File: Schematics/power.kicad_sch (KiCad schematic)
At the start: 12 parts, among them Q6 Q_PMOS_GSD, U3 PowerIn, U4 LDL1117-3.3

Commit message: updated to KiCad 10.0, updated .gitignore
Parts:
- C19: LCSC C2932476 -> C15850
- R30: LCSC C2933415 -> C17713
- U3: now left out of the parts list
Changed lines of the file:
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@@
 		(unit 1)
 		(exclude_from_sim no)
-		(in_bom yes)
+		(in_bom no)
 		(on_board yes)
 		(dnp no)
@@
 			)
 		)
-		(property "LCSC" "C2933415"
+		(property "LCSC" "C17713"
 			(at 99.06 86.36 0)
 			(effects
@@
 			)
 		)
-		(property "LCSC" "C2932476"
+		(property "LCSC" "C15850"
 			(at 210.82 105.41 0)
 			(effects

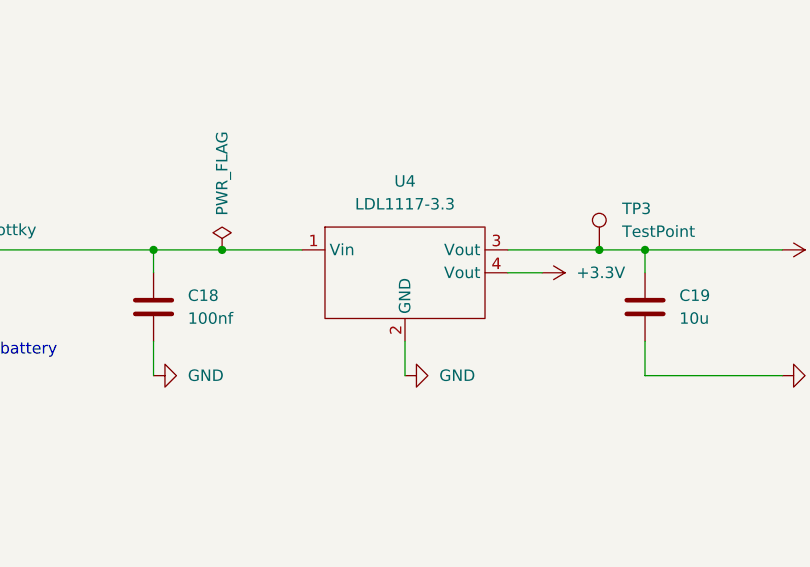
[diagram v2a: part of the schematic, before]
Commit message: Fixing ldo pinout, updated lora drivers need to still write final function such as lora sleep ect
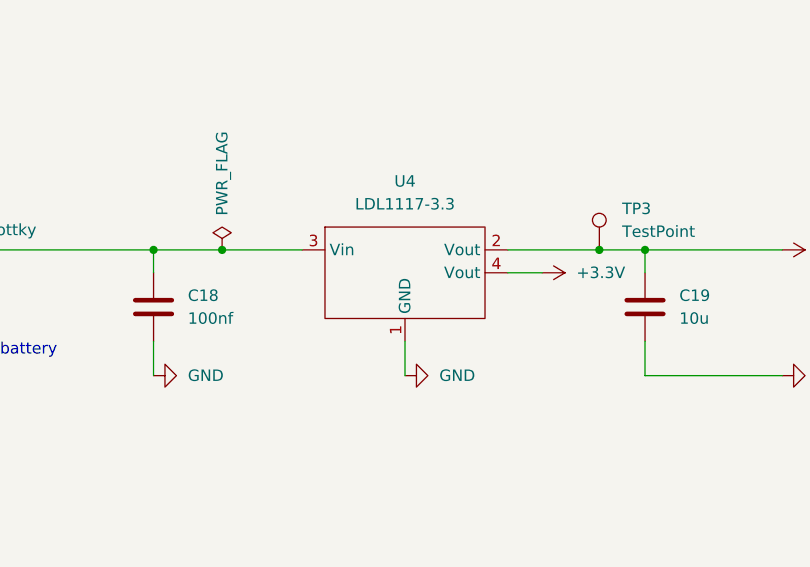
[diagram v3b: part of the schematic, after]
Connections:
- net +3.3V: now also U4.2 (Vout); no longer U4.3 (Vout)
- net GND: now also U4.1 (GND); no longer U4.2 (GND)
- net at C18.1, D2.1 (K), D3.1 (K): now also U4.3 (Vin); no longer U4.1 (Vin)
